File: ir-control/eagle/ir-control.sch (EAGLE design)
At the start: 35 parts, among them J1 MICRO USB, J2 MICRO USB, J3 MICRO USB, J4 SJ1-3523NG, Q1 DTA114EET1G (2x10K), Q2 12Mhz, Q3 MMBT2222A, U1 NUF2042XV6T1G, U2 MCP1754ST-3302E/CB, U3 LPC11U35FHI33/501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

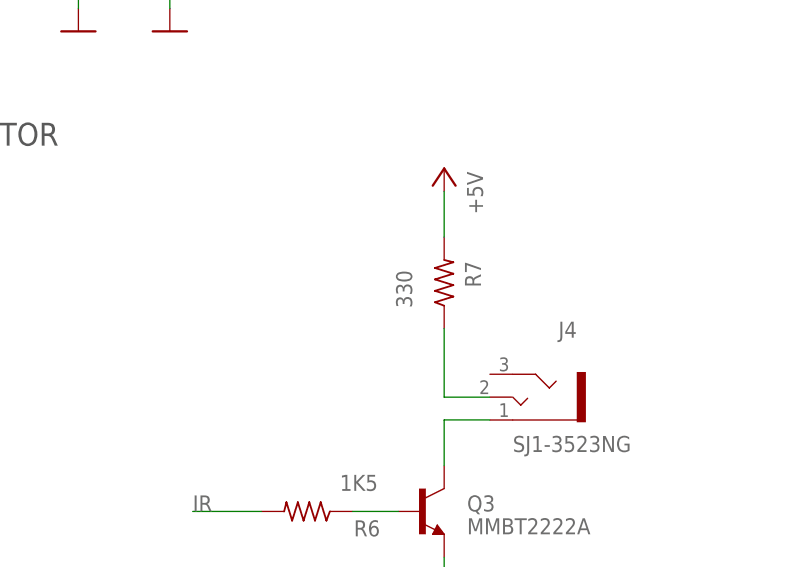
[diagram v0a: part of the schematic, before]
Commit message: Minor tweaks, change IR resistor from 330R to 100R, reduce IR TX timeout.
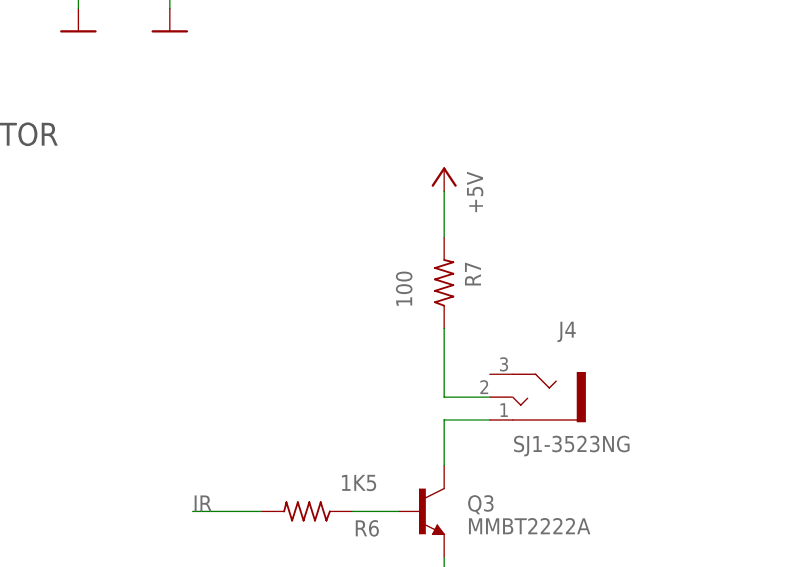
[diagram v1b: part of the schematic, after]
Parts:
- R7: value 330 -> 100
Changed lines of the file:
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@@
 <part name="J4" library="ir-control" deviceset="JACK" device="X" value="SJ1-3523NG"/>
 <part name="+5V3" library="ir-control" deviceset="+5V" device=""/>
-<part name="R7" library="ir-control" deviceset="R" device="R0402" value="330"/>
+<part name="R7" library="ir-control" deviceset="R" device="R0402" value="100"/>
 <part name="GND14" library="ir-control" deviceset="GND" device=""/>
 <part name="Q3" library="ir-control" deviceset="NPN" device="" value="MMBT2222A"/>
